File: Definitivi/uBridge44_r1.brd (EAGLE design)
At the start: 39.6 x 39.6 mm, 18 parts

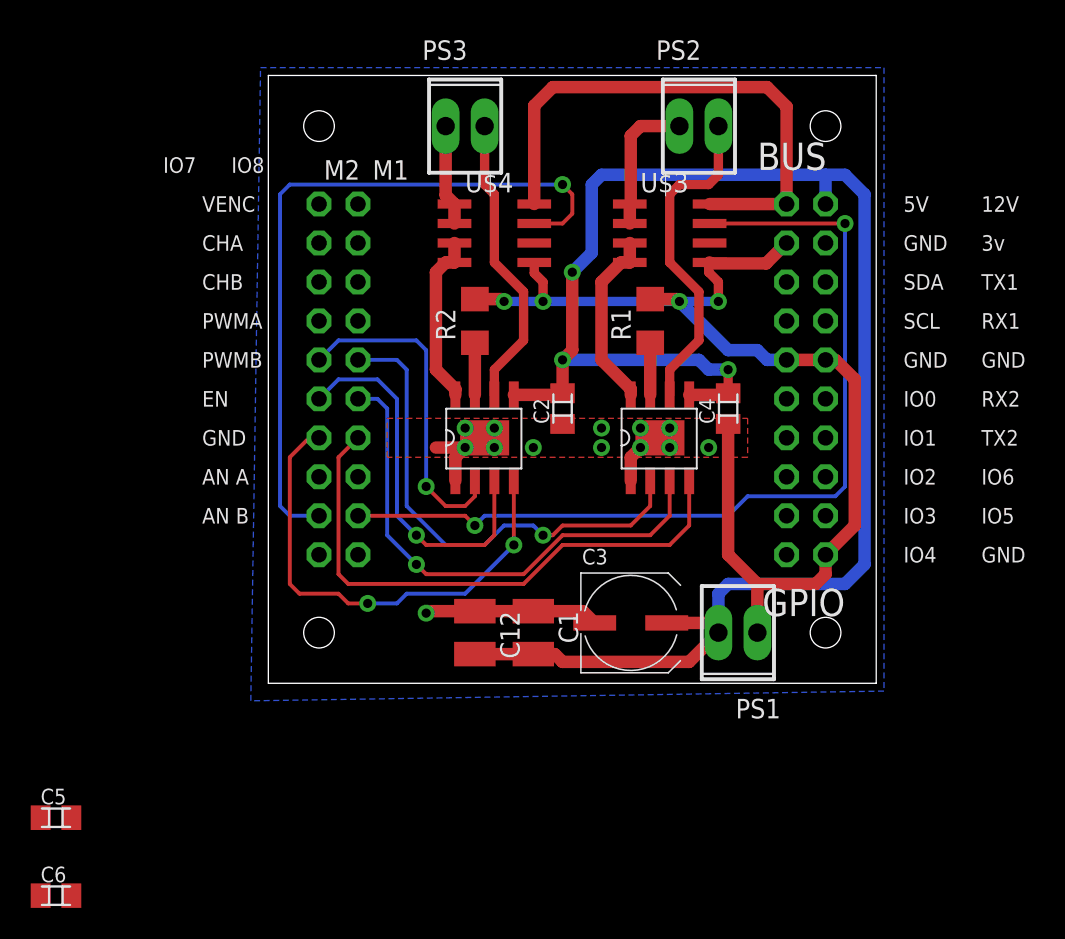
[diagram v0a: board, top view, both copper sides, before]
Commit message: Add filter on ACS / Update with ACS filter and GND top layer / @katodo i suggest to check files
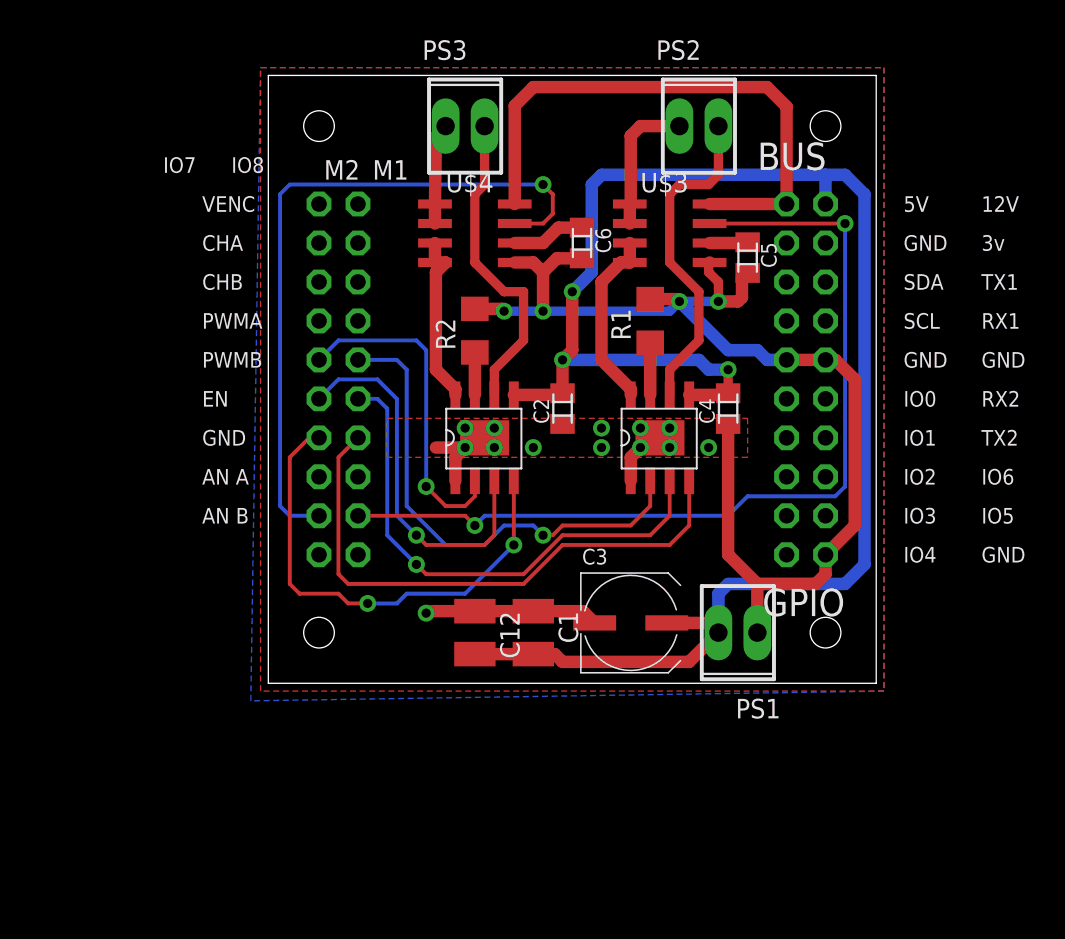
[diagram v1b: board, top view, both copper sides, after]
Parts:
- moved C5 58.0 mm to (31.8, 28.3), turned to 270 degrees
- moved C6 54.6 mm to (21.0, 29.2), turned to 270 degrees
- moved U$4 1.27 mm to (14.0, 29.8)
- moved R2 0.63 mm to (14.0, 23.5)
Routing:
- net N$5: track 0.00 -> 4.80 mm
- net GND: track 93.4 -> 96.2 mm
- net N$4: track 0.00 -> 2.48 mm
- net N$2: track 19.4 -> 20.6 mm
- net +5V: track 35.3 -> 36.5 mm
- net ANA2: track 46.7 -> 45.4 mm
- net N$1: track 3.40 -> 2.76 mm

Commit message: encoder connettor for motor / @katodo ready for you
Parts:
- added JP1, JP2: (no value), pinhead:2X02
- moved PS3 2.54 mm to (10.8, 36.8)
- moved PS2 2.54 mm to (31.1, 36.8)
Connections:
- removed net VENC1: SV2.3
- removed net VENC2: SV2.4
- new net VENC: JP1.3, JP2.3, SV2.3, SV2.4
- net CHA1: now also JP2.2
- net CHA2: now also JP1.2
- net CHB1: now also JP2.4
- net CHB2: now also JP1.4
- net GND: now also JP1.1, JP2.1
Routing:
- net +5V: track 36.5 -> 5.02 mm
- net N$6: track 9.18 -> 1.35 mm
- net N$8: track 21.5 -> 24.1 mm
- net ANA2: track 45.4 -> 47.2 mm
- net N$2: track 20.6 -> 21.2 mm
- net N$9: track 6.60 -> 7.11 mm
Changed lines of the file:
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@@
 <element name="R1" library="rcl" package="R1206" value="0R25" x="25.4" y="24.13" rot="R90"/>
 <element name="C2" library="rcl" package="C0805K" value="220nF" x="19.685" y="18.415" rot="R90"/>
-<element name="PS2" library="Personale" package="2POL254" value="" x="28.575" y="36.83"/>
+<element name="PS2" library="Personale" package="2POL254" value="" x="31.115" y="36.83"/>
 <element name="U$2" library="allegro" package="SOICN" value="A4950" x="14.605" y="16.51"/>
 <element name="R2" library="rcl" package="R1206" value="0R25" x="13.97" y="23.495" rot="R90"/>
 <element name="C4" library="rcl" package="C0805K" value="220nF" x="30.48" y="18.415" rot="R90"/>
-<element name="PS3" library="Personale" package="2POL254" value="" x="13.335" y="36.83"/>
+<element name="PS3" library="Personale" package="2POL254" value="" x="10.795" y="36.83"/>
 <element name="U$3" library="allegro" package="SO08" value="ACS723" x="26.67" y="29.845" rot="R270"/>
 <element name="U$4" library="allegro" package="SO08" value="ACS723" x="13.97" y="29.845" rot="R270"/>
@@
 <element name="C5" library="rcl" package="C0805K" value="1nF" x="31.75" y="28.2575" rot="R270"/>
 <element name="C6" library="rcl" package="C0805K" value="1nF" x="20.955" y="29.21" rot="R270"/>
+<element name="JP1" library="pinhead" package="2X02" value="" x="16.51" y="36.83"/>
+<element name="JP2" library="pinhead" package="2X02" value="" x="25.4" y="36.83"/>
 </elements>
 <signals>
@@
 <contactref element="U$3" pad="8"/>
 <contactref element="U$4" pad="8"/>
-<wire x1="16.57" y1="31.75" x2="16.57" y2="38.16" width="0.8128" layer="1"/>
-<wire x1="16.57" y1="38.16" x2="17.78" y2="39.37" width="0.8128" layer="1"/>
-<wire x1="17.78" y1="39.37" x2="33.02" y2="39.37" width="0.8128" layer="1"/>
-<wire x1="33.02" y1="39.37" x2="34.29" y2="38.1" width="0.8128" layer="1"/>
-<wire x1="34.29" y1="38.1" x2="34.29" y2="31.75" width="0.8128" layer="1"/>
 <wire x1="29.27" y1="31.75" x2="34.29" y2="31.75" width="0.8128" layer="1"/>
+<wire x1="16.57" y1="31.75" x2="29.27" y2="31.75" width="0" layer="19" extent="1-1"/>
 </signal>
 <signal name="+12V">
@@
 <vertex x="40.64" y="0"/>
 </polygon>
+<contactref element="JP1" pad="1"/>
+<contactref element="JP2" pad="1"/>
 </signal>
 <signal name="TX2">
@@
 <contactref element="SV2" pad="1"/>
 </signal>
-<signal name="VENC1">
-<contactref element="SV2" pad="3"/>
-</signal>
 <signal name="CHA1">
 <contactref element="SV2" pad="5"/>
+<contactref element="JP2" pad="2"/>
+<wire x1="6.35" y1="26.67" x2="24.13" y2="38.1" width="0" layer="19" extent="1-1"/>
 </signal>
 <signal name="CHB1">
 <contactref element="SV2" pad="7"/>
+<contactref element="JP2" pad="4"/>
+<wire x1="6.35" y1="24.13" x2="26.67" y2="38.1" width="0" layer="19" extent="1-1"/>
 </signal>
 <signal name="PWMA1">
@@
 <signal name="CHA2">
 <contactref element="SV2" pad="6"/>
+<contactref element="JP1" pad="2"/>
+<wire x1="3.81" y1="26.67" x2="15.24" y2="38.1" width="0" layer="19" extent="1-1"/>
 </signal>
 <signal name="CHB2">
 <contactref element="SV2" pad="8"/>
+<contactref element="JP1" pad="4"/>
+<wire x1="3.81" y1="24.13" x2="17.78" y2="38.1" width="0" layer="19" extent="1-1"/>
 </signal>
 <signal name="PWMA2">
@@
 <contactref element="SV2" pad="18"/>
 <contactref element="U$4" pad="7"/>
-<wire x1="18.415" y1="33.02" x2="19.05" y2="32.385" width="0.254" layer="1"/>
-<wire x1="19.05" y1="32.385" x2="19.05" y2="31.115" width="0.254" layer="1"/>
-<wire x1="19.05" y1="31.115" x2="18.415" y2="30.48" width="0.254" layer="1"/>
+<wire x1="20.32" y1="32.385" x2="18.415" y2="30.48" width="0.254" layer="1"/>
 <wire x1="18.415" y1="30.48" x2="16.57" y2="30.48" width="0.254" layer="1"/>
-<via x="18.415" y="33.02" extent="1-16" drill="0.6"/>
-<wire x1="18.415" y1="33.02" x2="1.905" y2="33.02" width="0.254" layer="16"/>
+<via x="20.32" y="32.385" extent="1-16" drill="0.6"/>
+<wire x1="20.32" y1="32.385" x2="19.685" y2="33.02" width="0.254" layer="16"/>
+<wire x1="19.685" y1="33.02" x2="1.905" y2="33.02" width="0.254" layer="16"/>
 <wire x1="1.905" y1="33.02" x2="1.27" y2="32.385" width="0.254" layer="16"/>
 <wire x1="1.27" y1="32.385" x2="1.27" y2="12.065" width="0.254" layer="16"/>
@@
 <contactref element="U$3" pad="1"/>
 <contactref element="PS2" pad="1"/>
-<wire x1="27.305" y1="36.83" x2="24.765" y2="36.83" width="0.8128" layer="1"/>
-<wire x1="24.765" y1="36.83" x2="24.13" y2="36.195" width="0.8128" layer="1"/>
-<wire x1="24.13" y1="36.195" x2="24.13" y2="31.81" width="0.8128" layer="1"/>
 <wire x1="24.13" y1="31.81" x2="24.07" y2="31.75" width="0.8128" layer="1"/>
 <wire x1="24.07" y1="31.75" x2="24.07" y2="30.48" width="0.8128" layer="1"/>
+<wire x1="24.13" y1="31.81" x2="29.845" y2="36.83" width="0" layer="19" extent="1-1"/>
 </signal>
 <signal name="N$9">
@@
 <contactref element="U$4" pad="1"/>
 <contactref element="PS3" pad="1"/>
-<wire x1="12.065" y1="36.83" x2="11.43" y2="36.135" width="0.8128" layer="1"/>
-<wire x1="11.43" y1="36.135" x2="11.37" y2="31.75" width="0.8128" layer="1"/>
+<wire x1="9.525" y1="36.83" x2="9.525" y2="33.595" width="0.8128" layer="1"/>
+<wire x1="9.525" y1="33.595" x2="11.37" y2="31.75" width="0.8128" layer="1"/>
 <wire x1="11.37" y1="31.75" x2="11.37" y2="30.48" width="0.8128" layer="1"/>
 </signal>
@@
 <wire x1="26.67" y1="27.94" x2="26.67" y2="32.385" width="0.6096" layer="1"/>
 <wire x1="26.67" y1="32.385" x2="27.305" y2="33.02" width="0.6096" layer="1"/>
-<wire x1="27.305" y1="33.02" x2="29.21" y2="33.02" width="0.6096" layer="1"/>
-<wire x1="29.21" y1="33.02" x2="29.845" y2="33.655" width="0.6096" layer="1"/>
-<wire x1="29.845" y1="33.655" x2="29.845" y2="36.83" width="0.6096" layer="1"/>
+<wire x1="27.305" y1="33.02" x2="31.75" y2="33.02" width="0.6096" layer="1"/>
+<wire x1="31.75" y1="33.02" x2="32.385" y2="33.655" width="0.6096" layer="1"/>
+<wire x1="32.385" y1="33.655" x2="32.385" y2="36.83" width="0.6096" layer="1"/>
 </signal>
 <signal name="N$2">
@@
 <wire x1="15.875" y1="26.035" x2="13.97" y2="27.94" width="0.6096" layer="1"/>
 <wire x1="13.97" y1="27.94" x2="13.97" y2="32.385" width="0.6096" layer="1"/>
-<wire x1="13.97" y1="32.385" x2="14.605" y2="33.02" width="0.6096" layer="1"/>
-<wire x1="14.605" y1="33.02" x2="14.605" y2="36.83" width="0.6096" layer="1"/>
-</signal>
-<signal name="VENC2">
+<wire x1="13.97" y1="32.385" x2="12.065" y2="34.29" width="0.6096" layer="1"/>
+<wire x1="12.065" y1="34.29" x2="12.065" y2="36.83" width="0.6096" layer="1"/>
+</signal>
+<signal name="VENC">
 <contactref element="SV2" pad="4"/>
+<contactref element="SV2" pad="3"/>
+<contactref element="JP1" pad="3"/>
+<contactref element="JP2" pad="3"/>
+<wire x1="17.78" y1="35.56" x2="26.67" y2="35.56" width="0" layer="19" extent="1-1"/>
+<wire x1="6.35" y1="29.21" x2="17.78" y2="35.56" width="0" layer="19" extent="1-1"/>
+<wire x1="3.81" y1="29.21" x2="6.35" y2="29.21" width="0" layer="19" extent="1-1"/>
 </signal>
 <signal name="N$4">
